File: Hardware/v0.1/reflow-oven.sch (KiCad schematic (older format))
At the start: 2 parts, among them U1 WeAct_MiniF4

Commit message: Finished schematics
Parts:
- added BZ1: HNB09A03, _AKL_Speaker:HNB09A03, symbol _AKL_Speaker:HNB09A03
- added C1: 100n, Capacitor_SMD:C_0603_1608Metric, symbol _AKL_Capacitor_603:100n
- added C2: 10n, Capacitor_SMD:C_0603_1608Metric, symbol _AKL_Capacitor_603:10n
- added D1, D2: MBR120VLSFT3G, _AKL_Diode:SOD-123FL, symbol _AKL_Diode:MBR120VLSFT3G
- added FB1, FB2: Ferrite_Bead, Inductor_SMD:L_0603_1608Metric, symbol Device:Ferrite_Bead
- added J1, J2, J3, J4: WJ124-3.81-2P, _AKL_Connector:WJ124-3.81-2P, symbol _AKL_Connector:WJ124-3.81-2P
- added Q1, Q2: FDN327N, Package_TO_SOT_SMD:SOT-23, symbol _AKL_Transistor:FDN327N
- added R1, R2, R3, R4, R5: 10K, Resistor_SMD:R_0603_1608Metric, symbol _AKL_Resistor_603:10K
- added SW1, SW2, SW3: TS-1095-A13B3-D1, Button_Switch_THT:SW_PUSH_6mm_H9.5mm, symbol _AKL_Switch:TS-1095-A13B3-D1
- added U2: MAX31855KASA+T, Package_SO:SOIC-8_3.9x4.9mm_P1.27mm, symbol _AKL_IC:MAX31855KASA+T
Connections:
- net BL: now reaches DS1.1 (BL)
- net BL: now also U1.32 (PA6)
- net RST: now reaches DS1.2 (RST)
- net RST: now also U1.29 (PA3)
- net DC: now reaches DS1.3 (DC)
- net DC: now also U1.28 (PA2)
- net CS1: now reaches DS1.4 (CS)
- net CS1: now also U1.30 (PA4)
- net SCK1: now reaches DS1.5 (CLK)
- net SCK1: now also U1.31 (PA5)
- net MOSI1: now reaches DS1.6 (DIN)
- net MOSI1: now also U1.33 (PA7)
- net GND: now reaches DS1.7 (GND)
- net GND: now also U1.19 (GND), U1.39 (GND), BZ1.2 (+), C1.2, J1.2 (Pin_2), Q1.2 (S), Q2.2 (S), R1.2, R2.2, R3.2, R4.2, R5.2, U2.1 (GND)
- net 3V3: now reaches DS1.8 (VCC)
- net 3V3: now also U1.20 (3V3), U1.38 (3V3), C1.1, SW1.2, SW2.2, SW3.2, U2.4 (VCC)
- net CS2: now reaches U1.1 (PB12)
- net CS2: now also U2.6 (~CS~)
- net OUT1: now reaches U1.13 (PB5)
- net OUT1: now also Q1.1 (G), R4.1
- net OUT2: now reaches U1.14 (PB6)
- net OUT2: now also Q2.1 (G), R5.1
- net 5V: now reaches U1.18 (5V)
- net 5V: now also U1.40 (5V), D1.1 (K), D2.1 (K), J1.1 (Pin_1), J3.1 (Pin_1), J4.1 (Pin_1)
- net SCK2: now reaches U1.2 (PB13)
- net SCK2: now also U2.5 (SCK)
- net BUZZER: now reaches U1.27 (PA1)
- net BUZZER: now also BZ1.1 (-)
- net MISO2: now reaches U1.3 (PB14)
- net MISO2: now also U2.7 (SO)
- net BTN_C: now reaches U1.34 (PB0)
- net BTN_C: now also R3.1, SW3.1
- net BTN_B: now reaches U1.35 (PB1)
- net BTN_B: now also R2.1, SW2.1
- net BTN_A: now reaches U1.37 (PB10)
- net BTN_A: now also R1.1, SW1.1
- new net OUT1-: D1.2 (A), J3.2 (Pin_2), Q1.3 (D)
- new net OUT2-: D2.2 (A), J4.2 (Pin_2), Q2.3 (D)
- new net T+: FB1.1, J2.1 (Pin_1)
- new net T+_FILTER: C2.1, FB1.2, U2.3 (T+)
- new net T-: FB2.1, J2.2 (Pin_2)
- new net T-_FILTER: C2.2, FB2.2, U2.2 (T-)
- no-connect marks 0 -> 19
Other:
- note removed: "To do:\n- 3 o 4 pulsadores\n- Buzzer activo a 3.3V\n- MAX31855/MAX6675\n- Conector entrada alimentacion 5V\n- Conectores termopar\n- Conector salida de activacion SSR, preferiblemente con MOSFET a 5V\n- Conectores extra por si acaso: segundo rele o ventilador\n- Ver si falta algo mas\n"
- moved on the sheet: DS1, U1

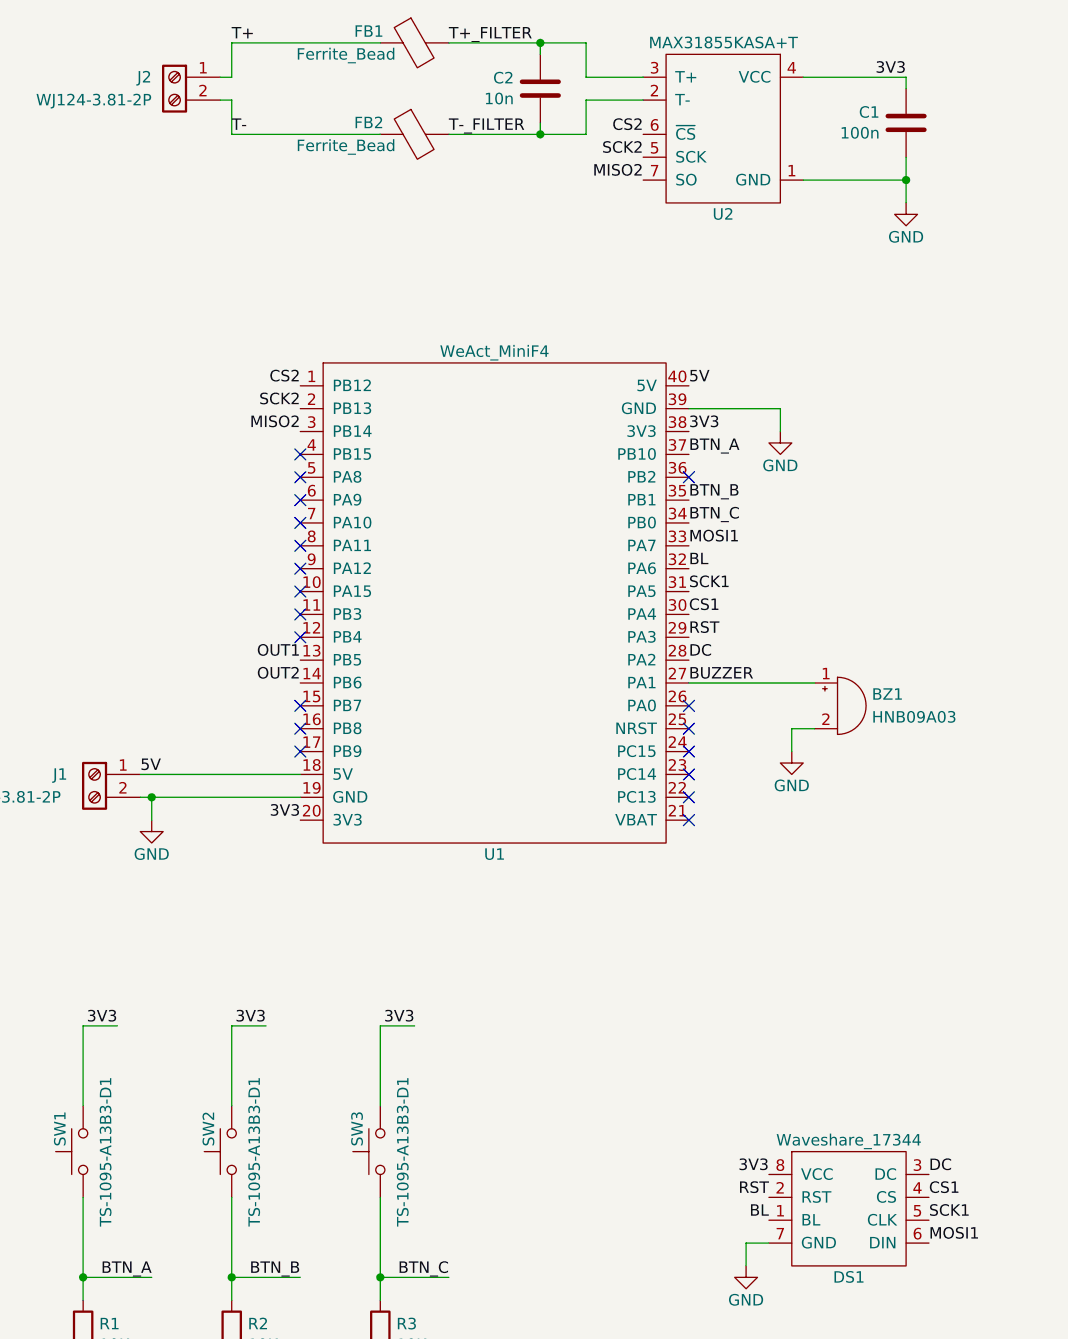
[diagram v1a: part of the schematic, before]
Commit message: Finished PCB layout
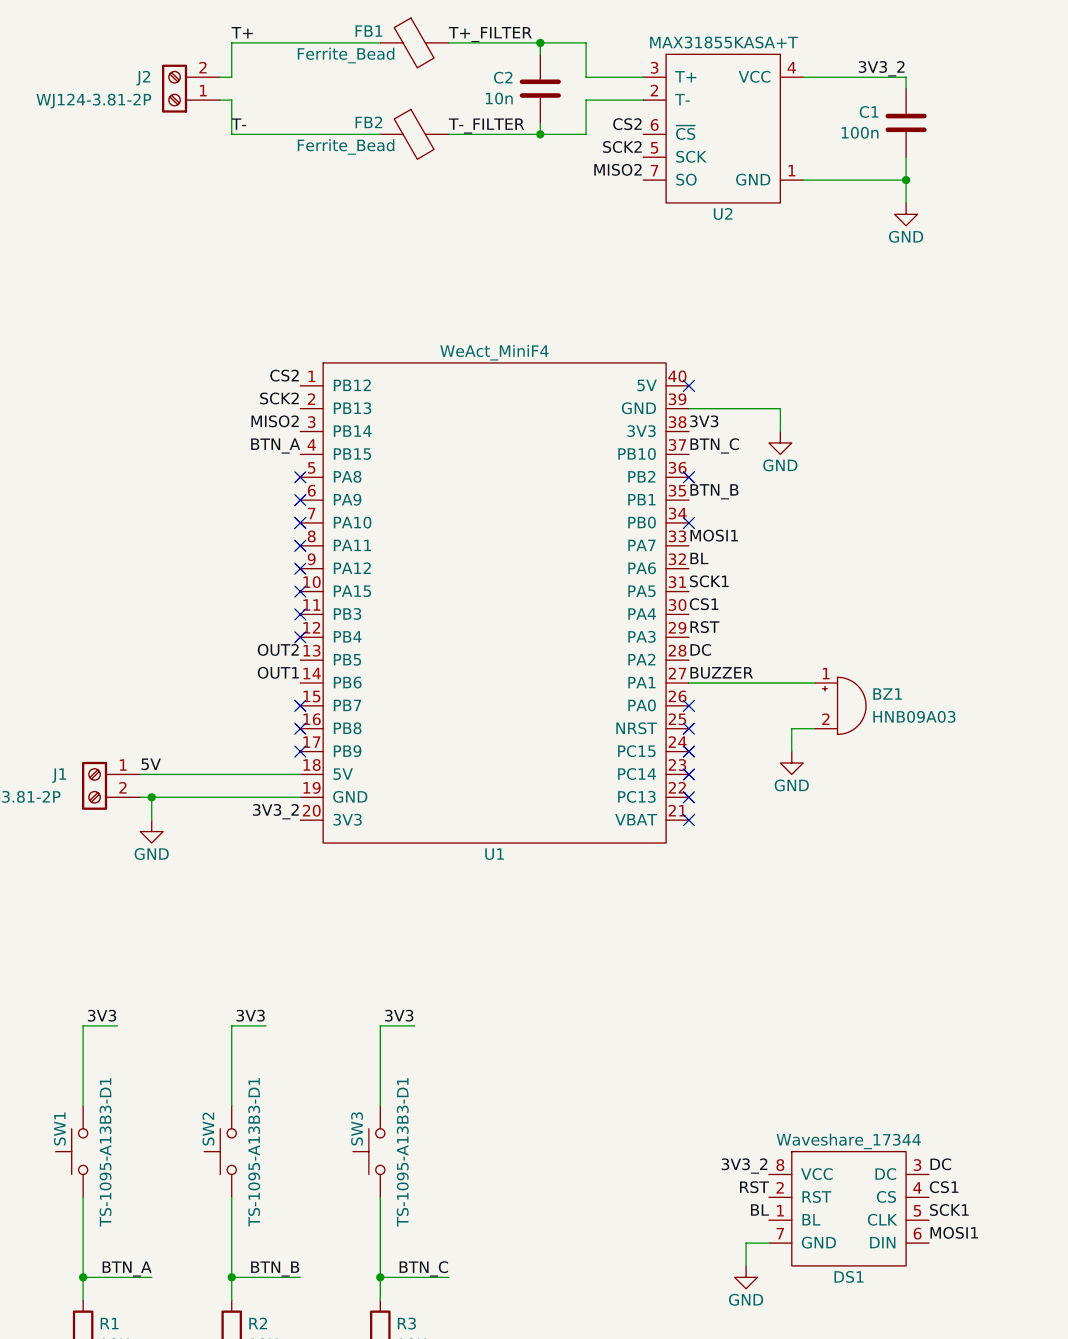
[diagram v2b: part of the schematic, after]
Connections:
- net 3V3: no longer C1.1, DS1.8 (VCC), U1.20 (3V3), U2.4 (VCC)
- net 5V: no longer U1.40 (5V)
- net BTN_A: now also U1.4 (PB15); no longer U1.37 (PB10)
- net BTN_C: now also U1.37 (PB10); no longer U1.34 (PB0)
- net OUT1: now also U1.14 (PB6); no longer U1.13 (PB5)
- net OUT2: now also U1.13 (PB5); no longer U1.14 (PB6)
- net T+: now also J2.2 (Pin_2); no longer J2.1 (Pin_1)
- net T-: now also J2.1 (Pin_1); no longer J2.2 (Pin_2)
- new net 3V3_2: C1.1, DS1.8 (VCC), U1.20 (3V3), U2.4 (VCC)
- no-connect marks 19 -> 20
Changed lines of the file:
@@
 	5700 1700 5700 1800
 Text Label 5700 1250 2    50   ~ 0
-3V3
+3V3_2
 Wire Wire Line
 	4550 1350 4300 1350
@@
 L _AKL_Connector:WJ124-3.81-2P J2
 U 1 1 5FE5C187
-P 2500 1250
+P 2500 1350
 F 0 "J2" H 2600 1250 50  0000 L CNN
-F 1 "WJ124-3.81-2P" H 2600 1150 50  0000 L CNN
-F 2 "_AKL_Connector:WJ124-3.81-2P" H 2500 1250 50  0001 C CNN
-F 3 "https://lcsc.com/product-detail/Pluggable-System-Terminal-Block_Ningbo-Kangnex-Elec-WJ124-3-81-2P_C69811.html" H 2500 1250 50  0001 C CNN
-F 4 "WJ124-3.81-2P" H 2500 1250 50  0001 C CNN "MPN"
-	1    2500 1250
-	-1   0    0    -1
+F 1 "WJ124-3.81-2P" H 2600 1350 50  0000 L CNN
+F 2 "_AKL_Connector:WJ124-3.81-2P" H 2500 1350 50  0001 C CNN
+F 3 "https://lcsc.com/product-detail/Pluggable-System-Terminal-Block_Ningbo-Kangnex-Elec-WJ124-3-81-2P_C69811.html" H 2500 1350 50  0001 C CNN
+F 4 "WJ124-3.81-2P" H 2500 1350 50  0001 C CNN "MPN"
+	1    2500 1350
+	-1   0    0    1
 $EndComp
 $Comp
@@
 Wire Wire Line
 	2350 4300 3050 4300
-Text Label 3050 4500 2    50   ~ 0
-3V3
 Text Label 4750 2800 0    50   ~ 0
 3V3
-Text Label 4750 2600 0    50   ~ 0
-5V
 Wire Wire Line
 	2350 4400 2400 4400
@@
 Text Label 3550 5400 2    50   ~ 0
 3V3
-Text Label 4750 2900 0    50   ~ 0
+Text Label 3050 2900 2    50   ~ 0
 BTN_A
 Text Label 4750 3100 0    50   ~ 0
 BTN_B
-Text Label 4750 3200 0    50   ~ 0
+Text Label 4750 2900 0    50   ~ 0
 BTN_C
 $Comp
@@
 Wire Wire Line
 	5200 4100 5300 4100
+Text Label 3050 3900 2    50   ~ 0
+OUT1
 Text Label 3050 3800 2    50   ~ 0
-OUT1
-Text Label 3050 3900 2    50   ~ 0
 OUT2
 Text Label 3050 2600 2    50   ~ 0
@@
 	5000 6350 5000 6450
 Text Label 5100 6050 2    50   ~ 0
-3V3
+3V3_2
 Text Label 5800 6050 0    50   ~ 0
 DC
@@
 BUZZER
 NoConn ~ 4750 4000
-NoConn ~ 3050 2900
 NoConn ~ 3050 4000
 NoConn ~ 3050 4100
@@
 Wire Wire Line
 	10700 6100 10700 6150
+NoConn ~ 4750 2600
+NoConn ~ 4750 3200
+Text Label 3050 4500 2    50   ~ 0
+3V3_2
 $EndSCHEMATC
